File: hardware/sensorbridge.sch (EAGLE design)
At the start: 25 parts

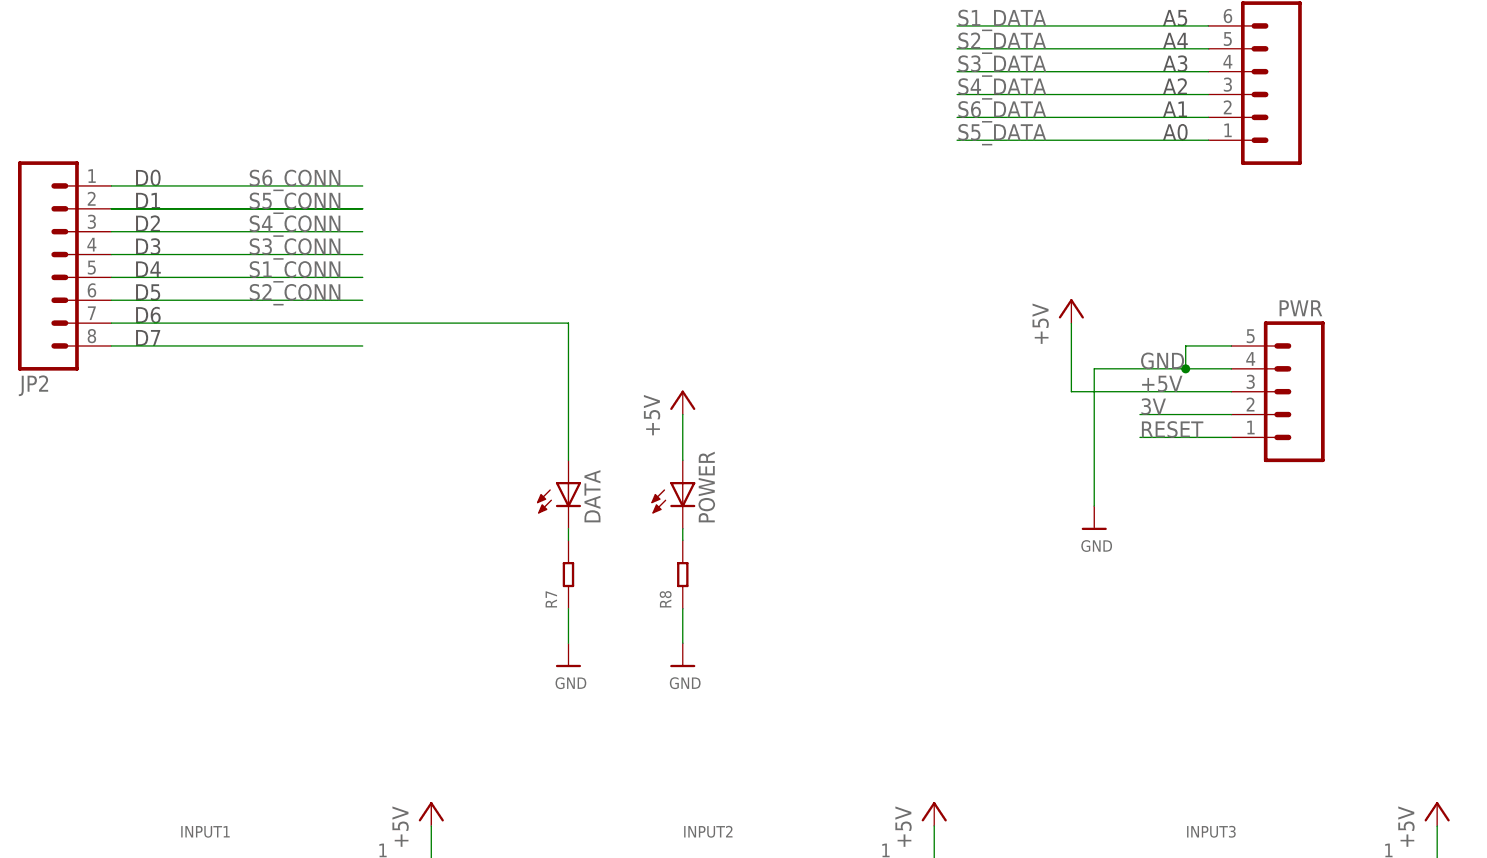
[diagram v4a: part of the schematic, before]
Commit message: Digital pin reconfiguration
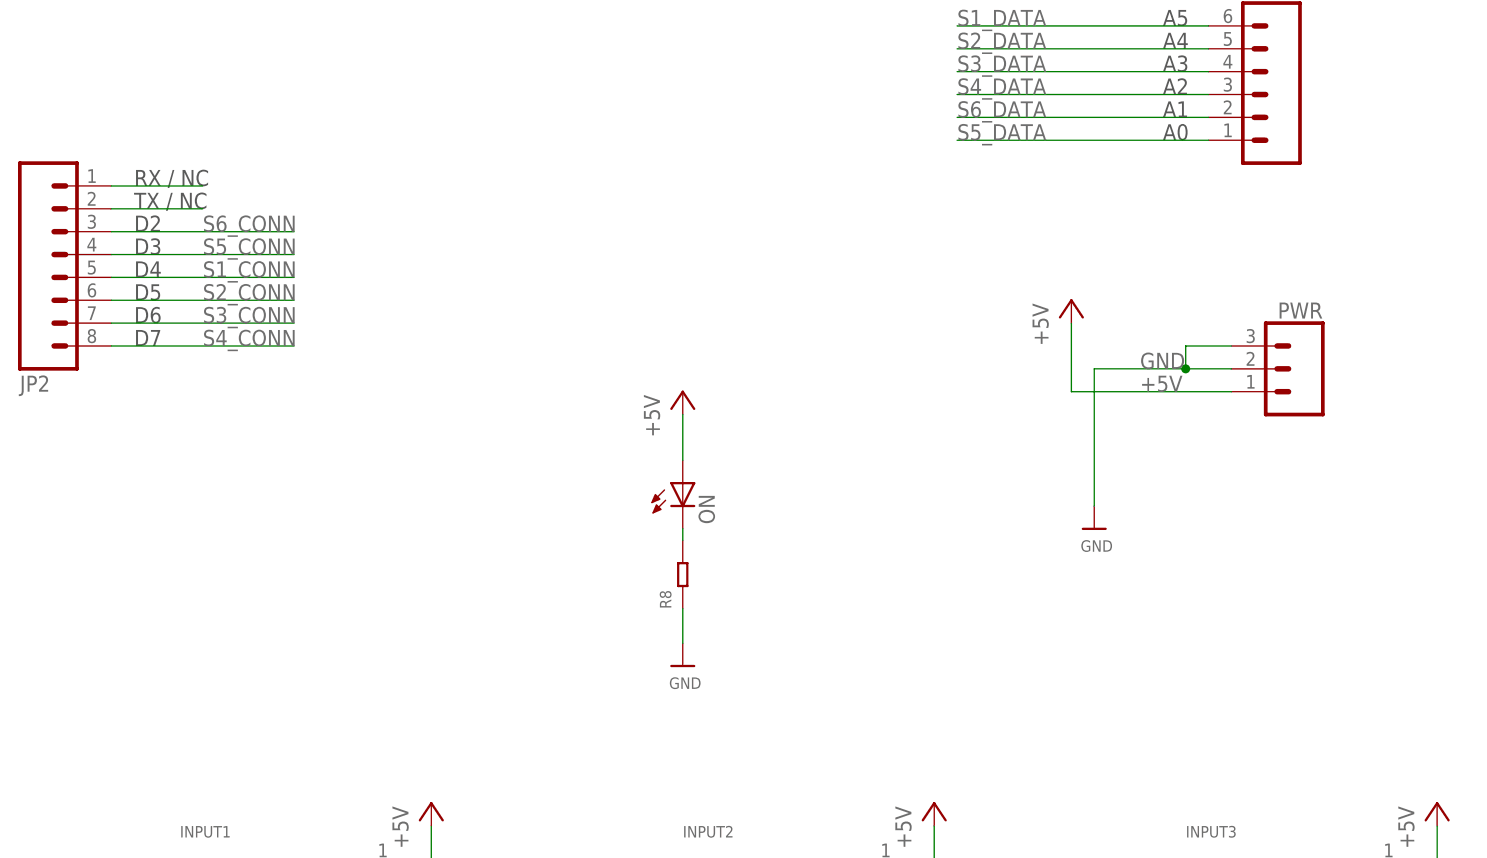
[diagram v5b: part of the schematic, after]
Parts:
- removed DATA: (no value), adafruit:LEDCHIP-LED0603
- removed R7: (no value), Seeed-OPL-Resistor:RES-0603
- PWR: device SparkFun-Connectors:M05NO_SILK -> SparkFun-Connectors:CONN_03
- renumbered POWER to ON
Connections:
- removed net 3V: PWR.2
- removed net N$10: JP2.8
- removed net N$7: DATA.C, R7.2
- removed net N$8: DATA.A, JP2.7
- removed net RESET: PWR.1
- new net N$12: JP2.2
- new net N$13: JP2.1
- net +5V: now also PWR.1; no longer PWR.3
- net GND: now also PWR.2, PWR.3; no longer PWR.4, PWR.5, R7.1
- net S3_CONN: now also JP2.7; no longer JP2.4
- net S4_CONN: now also JP2.8; no longer JP2.3
- net S5_CONN: now also JP2.4; no longer JP2.2
- net S6_CONN: now also JP2.3; no longer JP2.1
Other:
- note added: "RX / NC"
- note added: "TX / NC"
- note removed: "D0"
- note removed: "D1"
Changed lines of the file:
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@@
 <part name="ANALOG" library="SparkFun-Connectors" deviceset="M06" device="NO_SILK_FEMALE_PTH"/>
 <part name="JP2" library="SparkFun-Connectors" deviceset="M08" device="NO_SILK_FEMALE_PTH"/>
-<part name="PWR" library="SparkFun-Connectors" deviceset="M05" device="NO_SILK"/>
-<part name="DATA" library="adafruit" deviceset="LED" device="CHIP-LED0603"/>
-<part name="R7" library="Seeed-OPL-Resistor" deviceset="RES" device="-0603"/>
-<part name="U$2" library="microbuilder" deviceset="GND" device=""/>
-<part name="POWER" library="adafruit" deviceset="LED" device="CHIP-LED0603"/>
+<part name="ON" library="adafruit" deviceset="LED" device="CHIP-LED0603"/>
 <part name="R8" library="Seeed-OPL-Resistor" deviceset="RES" device="-0603"/>
 <part name="U$15" library="microbuilder" deviceset="GND" device=""/>
 <part name="P+8" library="supply1" deviceset="+5V" device=""/>
+<part name="PWR" library="SparkFun-Connectors" deviceset="CONN_03" device=""/>
 </parts>
 <sheets>
@@
 <text x="111.76" y="83.82" size="1.778" layer="97">A4</text>
 <text x="111.76" y="86.36" size="1.778" layer="97">A5</text>
-<text x="-2.54" y="68.58" size="1.778" layer="97">D0</text>
-<text x="-2.54" y="66.04" size="1.778" layer="97">D1</text>
+<text x="-2.54" y="68.58" size="1.778" layer="97">RX / NC</text>
+<text x="-2.54" y="66.04" size="1.778" layer="97">TX / NC</text>
 <text x="-2.54" y="63.5" size="1.778" layer="97">D2</text>
 <text x="-2.54" y="60.96" size="1.778" layer="97">D3</text>
@@
 <instance part="ANALOG" gate="G$1" x="121.92" y="78.74" rot="MR0"/>
 <instance part="JP2" gate="G$1" x="-10.16" y="60.96" rot="MR180"/>
-<instance part="PWR" gate="G$1" x="127" y="45.72" rot="MR0"/>
-<instance part="DATA" gate="G$1" x="45.72" y="35.56"/>
-<instance part="R7" gate="R" x="45.72" y="25.4" rot="R90"/>
-<instance part="U$2" gate="G$1" x="45.72" y="15.24"/>
-<instance part="POWER" gate="G$1" x="58.42" y="35.56"/>
+<instance part="ON" gate="G$1" x="58.42" y="35.56"/>
 <instance part="R8" gate="R" x="58.42" y="25.4" rot="R90"/>
 <instance part="U$15" gate="G$1" x="58.42" y="15.24"/>
 <instance part="P+8" gate="1" x="58.42" y="45.72"/>
+<instance part="PWR" gate="J$1" x="127" y="48.26" rot="MR0"/>
 </instances>
 <busses>
@@
 <label x="109.22" y="48.26" size="1.778" layer="95"/>
 <wire x1="114.3" y1="48.26" x2="114.3" y2="50.8" width="0.1524" layer="91"/>
+<junction x="114.3" y="48.26"/>
+<pinref part="PWR" gate="J$1" pin="2"/>
+<wire x1="114.3" y1="48.26" x2="119.38" y2="48.26" width="0.1524" layer="91"/>
+<pinref part="PWR" gate="J$1" pin="3"/>
 <wire x1="114.3" y1="50.8" x2="119.38" y2="50.8" width="0.1524" layer="91"/>
-<junction x="114.3" y="48.26"/>
-<pinref part="PWR" gate="G$1" pin="4"/>
-<wire x1="114.3" y1="48.26" x2="119.38" y2="48.26" width="0.1524" layer="91"/>
-<pinref part="PWR" gate="G$1" pin="5"/>
-</segment>
-<segment>
-<pinref part="U$2" gate="G$1" pin="GND"/>
-<pinref part="R7" gate="R" pin="1"/>
-<wire x1="45.72" y1="17.78" x2="45.72" y2="21.59" width="0.1524" layer="91"/>
 </segment>
 <segment>
@@
 <pinref part="P+7" gate="1" pin="+5V"/>
 <wire x1="101.6" y1="45.72" x2="101.6" y2="53.34" width="0.1524" layer="91"/>
+<label x="109.22" y="45.72" size="1.778" layer="95"/>
+<pinref part="PWR" gate="J$1" pin="1"/>
 <wire x1="101.6" y1="45.72" x2="119.38" y2="45.72" width="0.1524" layer="91"/>
-<label x="109.22" y="45.72" size="1.778" layer="95"/>
-<pinref part="PWR" gate="G$1" pin="3"/>
 </segment>
 <segment>
 <pinref part="P+8" gate="1" pin="+5V"/>
-<pinref part="POWER" gate="G$1" pin="A"/>
+<pinref part="ON" gate="G$1" pin="A"/>
 <wire x1="58.42" y1="43.18" x2="58.42" y2="38.1" width="0.1524" layer="91"/>
 </segment>
@@
 </segment>
 <segment>
-<label x="10.16" y="58.42" size="1.778" layer="95"/>
 <pinref part="JP2" gate="G$1" pin="5"/>
-<wire x1="22.86" y1="58.42" x2="-5.08" y2="58.42" width="0.1524" layer="91"/>
+<wire x1="-5.08" y1="58.42" x2="15.24" y2="58.42" width="0.1524" layer="91"/>
+<label x="5.08" y="58.42" size="1.778" layer="95"/>
 </segment>
 </net>
@@
 </segment>
 <segment>
-<label x="10.16" y="55.88" size="1.778" layer="95"/>
 <pinref part="JP2" gate="G$1" pin="6"/>
-<wire x1="22.86" y1="55.88" x2="-5.08" y2="55.88" width="0.1524" layer="91"/>
+<wire x1="-5.08" y1="55.88" x2="15.24" y2="55.88" width="0.1524" layer="91"/>
+<label x="5.08" y="55.88" size="1.778" layer="95"/>
 </segment>
 </net>
@@
 </segment>
 <segment>
-<label x="10.16" y="60.96" size="1.778" layer="95"/>
-<pinref part="JP2" gate="G$1" pin="4"/>
-<wire x1="22.86" y1="60.96" x2="-5.08" y2="60.96" width="0.1524" layer="91"/>
+<pinref part="JP2" gate="G$1" pin="7"/>
+<wire x1="-5.08" y1="53.34" x2="15.24" y2="53.34" width="0.1524" layer="91"/>
+<label x="5.08" y="53.34" size="1.778" layer="95"/>
 </segment>
 </net>
@@
 </segment>
 <segment>
-<label x="10.16" y="63.5" size="1.778" layer="95"/>
-<pinref part="JP2" gate="G$1" pin="3"/>
-<wire x1="22.86" y1="63.5" x2="-5.08" y2="63.5" width="0.1524" layer="91"/>
+<pinref part="JP2" gate="G$1" pin="8"/>
+<wire x1="-5.08" y1="50.8" x2="15.24" y2="50.8" width="0.1524" layer="91"/>
+<label x="5.08" y="50.8" size="1.778" layer="95"/>
 </segment>
 </net>
@@
 </segment>
 <segment>
-<wire x1="-5.08" y1="66.04" x2="22.86" y2="66.04" width="0.1524" layer="91"/>
-<label x="10.16" y="66.04" size="1.778" layer="95"/>
-<pinref part="JP2" gate="G$1" pin="2"/>
-<wire x1="-5.08" y1="66.04" x2="22.86" y2="66.04" width="0.1524" layer="91"/>
+<pinref part="JP2" gate="G$1" pin="4"/>
+<wire x1="-5.08" y1="60.96" x2="15.24" y2="60.96" width="0.1524" layer="91"/>
+<label x="5.08" y="60.96" size="1.778" layer="95"/>
 </segment>
 </net>
@@
 </segment>
 <segment>
-<label x="10.16" y="68.58" size="1.778" layer="95"/>
-<pinref part="JP2" gate="G$1" pin="1"/>
-<wire x1="22.86" y1="68.58" x2="-5.08" y2="68.58" width="0.1524" layer="91"/>
+<pinref part="JP2" gate="G$1" pin="3"/>
+<wire x1="-5.08" y1="63.5" x2="15.24" y2="63.5" width="0.1524" layer="91"/>
+<label x="5.08" y="63.5" size="1.778" layer="95"/>
 </segment>
 </net>
@@
 </segment>
 </net>
-<net name="3V" class="0">
-<segment>
-<label x="109.22" y="43.18" size="1.778" layer="95"/>
-<pinref part="PWR" gate="G$1" pin="2"/>
-<wire x1="119.38" y1="43.18" x2="109.22" y2="43.18" width="0.1524" layer="91"/>
-</segment>
-</net>
-<net name="RESET" class="0">
-<segment>
-<label x="109.22" y="40.64" size="1.778" layer="95"/>
-<pinref part="PWR" gate="G$1" pin="1"/>
-<wire x1="109.22" y1="40.64" x2="119.38" y2="40.64" width="0.1524" layer="91"/>
-</segment>
-</net>
-<net name="N$7" class="0">
-<segment>
-<pinref part="R7" gate="R" pin="2"/>
-<pinref part="DATA" gate="G$1" pin="C"/>
-<wire x1="45.72" y1="29.21" x2="45.72" y2="30.48" width="0.1524" layer="91"/>
-</segment>
-</net>
-<net name="N$8" class="0">
-<segment>
-<pinref part="JP2" gate="G$1" pin="7"/>
-<wire x1="-5.08" y1="53.34" x2="45.72" y2="53.34" width="0.1524" layer="91"/>
-<pinref part="DATA" gate="G$1" pin="A"/>
-<wire x1="45.72" y1="53.34" x2="45.72" y2="38.1" width="0.1524" layer="91"/>
-</segment>
-</net>
 <net name="N$9" class="0">
 <segment>
-<pinref part="POWER" gate="G$1" pin="C"/>
+<pinref part="ON" gate="G$1" pin="C"/>
 <wire x1="58.42" y1="30.48" x2="58.42" y2="29.21" width="0.1524" layer="91"/>
 <pinref part="R8" gate="R" pin="2"/>
 </segment>
 </net>
-<net name="N$10" class="0">
-<segment>
-<pinref part="JP2" gate="G$1" pin="8"/>
-<wire x1="-5.08" y1="50.8" x2="22.86" y2="50.8" width="0.1524" layer="91"/>
-</segment>
-</net>
+<net name="N$12" class="0">
+<segment>
+<pinref part="JP2" gate="G$1" pin="2"/>
+<wire x1="-5.08" y1="66.04" x2="5.08" y2="66.04" width="0.1524" layer="91"/>
+</segment>
+</net>
+<net name="N$13" class="0">
+<segment>
+<pinref part="JP2" gate="G$1" pin="1"/>
+<wire x1="-5.08" y1="68.58" x2="5.08" y2="68.58" width="0.1524" layer="91"/>
+</segment>
+</net>

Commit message: Replaced header parts for headers with silkscreen
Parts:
- ANALOG: device SparkFun-Connectors:M06NO_SILK_FEMALE_PTH -> SparkFun-Connectors:M06SILK_FEMALE_PTH
- JP2: device SparkFun-Connectors:M08NO_SILK_FEMALE_PTH -> SparkFun-Connectors:M08
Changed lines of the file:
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@@
 <part name="P+7" library="supply1" deviceset="+5V" device=""/>
 <part name="U$14" library="microbuilder" deviceset="GND" device=""/>
-<part name="ANALOG" library="SparkFun-Connectors" deviceset="M06" device="NO_SILK_FEMALE_PTH"/>
-<part name="JP2" library="SparkFun-Connectors" deviceset="M08" device="NO_SILK_FEMALE_PTH"/>
+<part name="ANALOG" library="SparkFun-Connectors" deviceset="M06" device="SILK_FEMALE_PTH"/>
+<part name="JP2" library="SparkFun-Connectors" deviceset="M08" device=""/>
 <part name="ON" library="adafruit" deviceset="LED" device="CHIP-LED0603"/>
 <part name="R8" library="Seeed-OPL-Resistor" deviceset="RES" device="-0603"/>
